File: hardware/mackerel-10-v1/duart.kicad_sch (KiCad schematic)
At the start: 7 parts, among them J10 Conn_01x06, J9 Conn_01x06, U7 XR68C681, X2 3.6864MHz

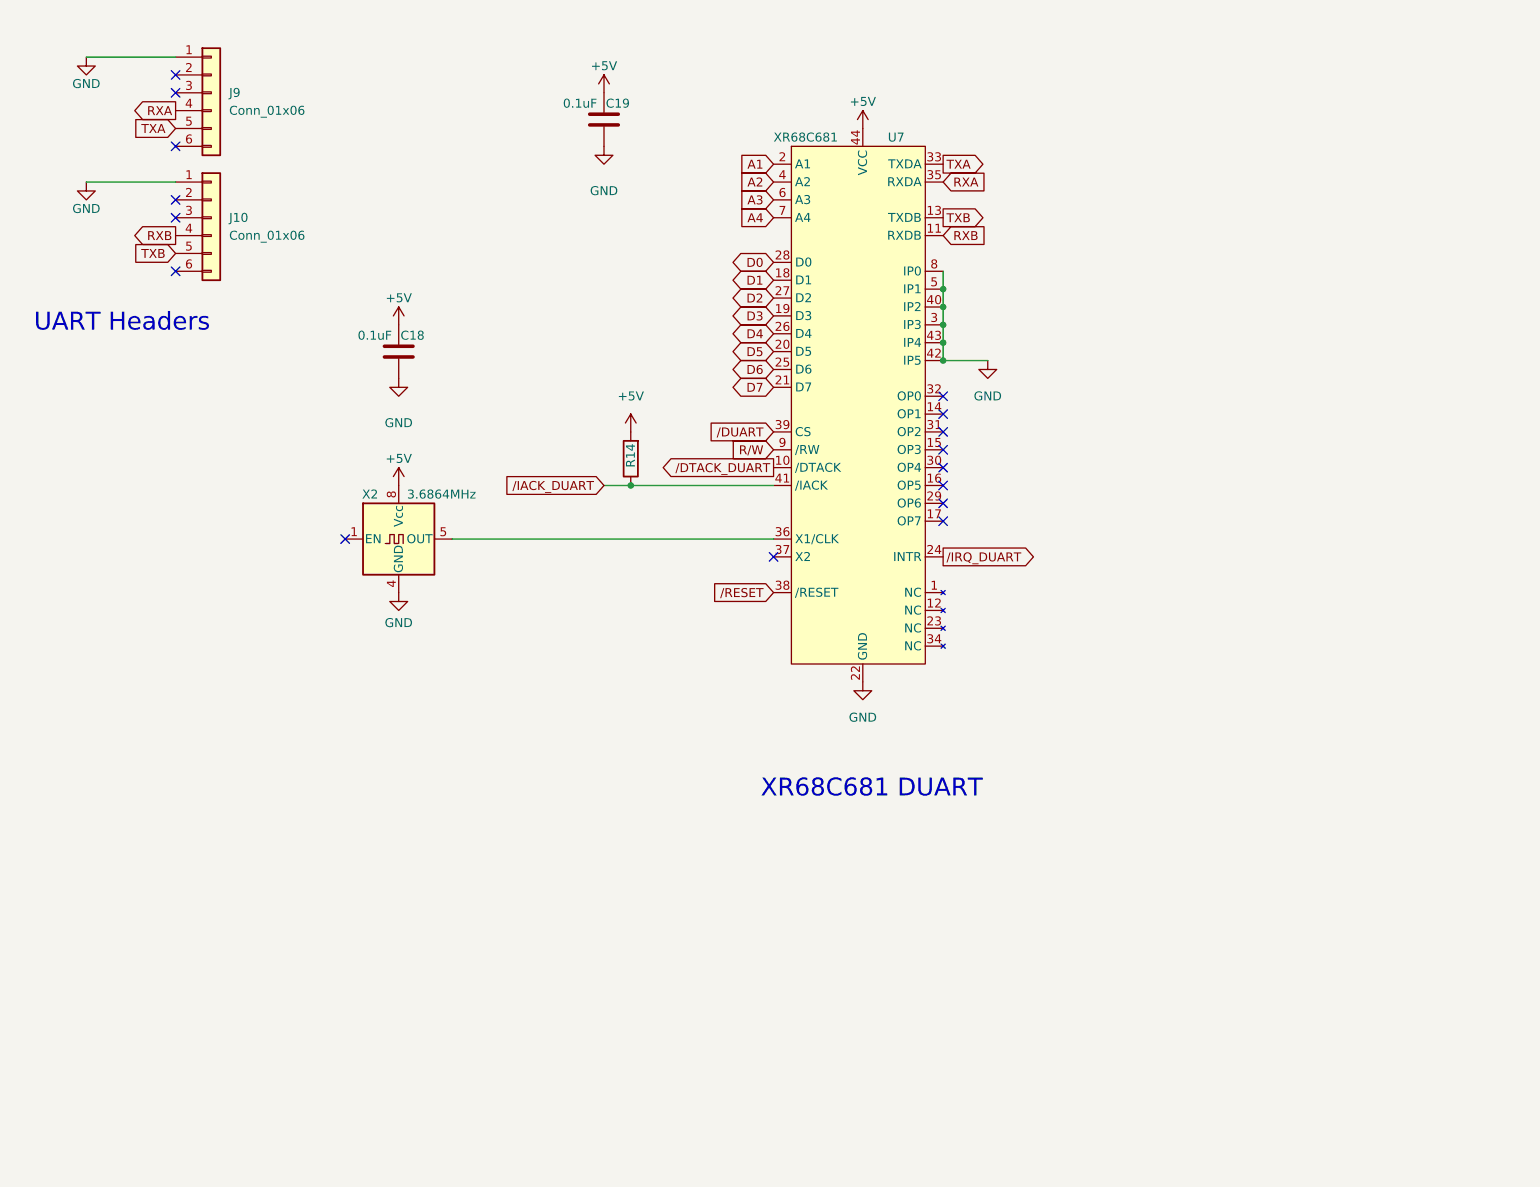
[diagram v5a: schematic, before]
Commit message: Mackerel-10 proto board ready for manufacturing
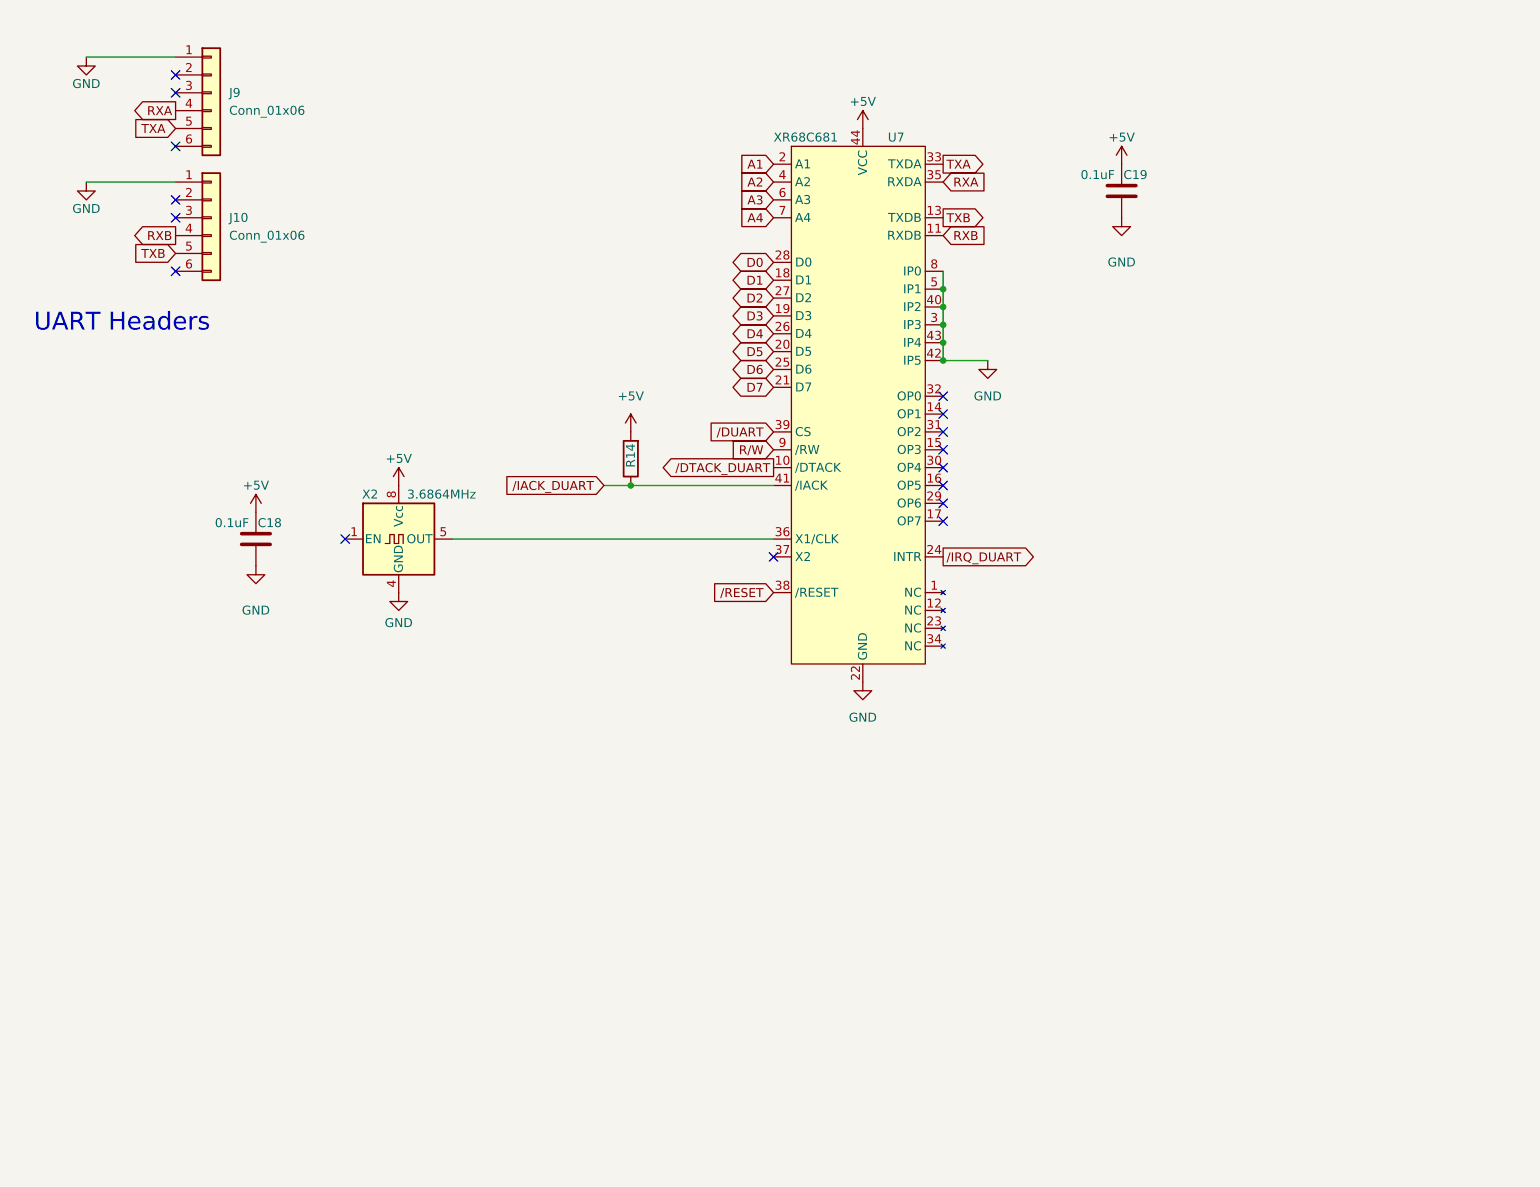
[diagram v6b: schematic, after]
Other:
- note removed: "XR68C681 DUART"
- moved on the sheet: C18, C19
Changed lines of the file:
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@@
-		)
-	)
-	(text "XR68C681 DUART"
-		(exclude_from_sim no)
-		(at 156.21 137.16 0)
-		(effects
-			(font
-				(size 2.54 2.54)
-			)
 		)
 	)
@@
 	(symbol
 		(lib_id "Device:C")
-		(at 88.9 74.93 0)
+		(at 68.58 101.6 0)
 		(unit 1)
 		(exclude_from_sim no)
@@
 		(dnp no)
 		(property "Reference" "C18"
-			(at 89.154 72.644 0)
+			(at 68.834 99.314 0)
 			(effects
 				(font
@@
 		)
 		(property "Value" "0.1uF"
-			(at 83.058 72.644 0)
+			(at 62.738 99.314 0)
 			(effects
 				(font
@@
 		)
 		(property "Footprint" "Capacitor_THT:C_Disc_D4.7mm_W2.5mm_P5.00mm"
-			(at 89.8652 78.74 0)
+			(at 69.5452 105.41 0)
 			(effects
 				(font
@@
 		)
 		(property "Datasheet" "~"
-			(at 88.9 74.93 0)
+			(at 68.58 101.6 0)
 			(effects
 				(font
@@
 		)
 		(property "Description" "Unpolarized capacitor"
-			(at 88.9 74.93 0)
+			(at 68.58 101.6 0)
 			(effects
 				(font
@@
 	(symbol
 		(lib_id "power:+5V")
-		(at 88.9 71.12 0)
+		(at 68.58 97.79 0)
 		(unit 1)
 		(exclude_from_sim no)
@@
 		(fields_autoplaced yes)
 		(property "Reference" "#PWR046"
-			(at 88.9 74.93 0)
+			(at 68.58 101.6 0)
 			(effects
 				(font
@@
 		)
 		(property "Value" "+5V"
-			(at 88.9 67.31 0)
+			(at 68.58 93.98 0)
 			(effects
 				(font
@@
 		)
 		(property "Footprint" ""
-			(at 88.9 71.12 0)
+			(at 68.58 97.79 0)
 			(effects
 				(font
@@
 		)
 		(property "Datasheet" ""
-			(at 88.9 71.12 0)
+			(at 68.58 97.79 0)
 			(effects
 				(font
@@
 		)
 		(property "Description" "Power symbol creates a global label with name \"+5V\""
-			(at 88.9 71.12 0)
+			(at 68.58 97.79 0)
 			(effects
 				(font
@@
 	(symbol
 		(lib_id "power:GND")
-		(at 118.11 45.72 0)
+		(at 191.77 55.88 0)
 		(unit 1)
 		(exclude_from_sim no)
@@
 		(fields_autoplaced yes)
 		(property "Reference" "#PWR068"
-			(at 118.11 52.07 0)
+			(at 191.77 62.23 0)
 			(effects
 				(font
@@
 		)
 		(property "Value" "GND"
-			(at 118.11 52.07 0)
+			(at 191.77 62.23 0)
 			(effects
 				(font
@@
 		)
 		(property "Footprint" ""
-			(at 118.11 45.72 0)
+			(at 191.77 55.88 0)
 			(effects
 				(font
@@
 		)
 		(property "Datasheet" ""
-			(at 118.11 45.72 0)
+			(at 191.77 55.88 0)
 			(effects
 				(font
@@
 		)
 		(property "Description" "Power symbol creates a global label with name \"GND\" , ground"
-			(at 118.11 45.72 0)
+			(at 191.77 55.88 0)
 			(effects
 				(font
@@
 	(symbol
 		(lib_id "power:GND")
-		(at 88.9 78.74 0)
+		(at 68.58 105.41 0)
 		(unit 1)
 		(exclude_from_sim no)
@@
 		(fields_autoplaced yes)
 		(property "Reference" "#PWR047"
-			(at 88.9 85.09 0)
+			(at 68.58 111.76 0)
 			(effects
 				(font
@@
 		)
 		(property "Value" "GND"
-			(at 88.9 85.09 0)
+			(at 68.58 111.76 0)
 			(effects
 				(font
@@
 		)
 		(property "Footprint" ""
-			(at 88.9 78.74 0)
+			(at 68.58 105.41 0)
 			(effects
 				(font
@@
 		)
 		(property "Datasheet" ""
-			(at 88.9 78.74 0)
+			(at 68.58 105.41 0)
 			(effects
 				(font
@@
 		)
 		(property "Description" "Power symbol creates a global label with name \"GND\" , ground"
-			(at 88.9 78.74 0)
+			(at 68.58 105.41 0)
 			(effects
 				(font
@@
 	(symbol
 		(lib_id "Device:C")
-		(at 118.11 41.91 0)
+		(at 191.77 52.07 0)
 		(unit 1)
 		(exclude_from_sim no)
@@
 		(dnp no)
 		(property "Reference" "C19"
-			(at 118.364 39.624 0)
+			(at 192.024 49.784 0)
 			(effects
 				(font
@@
 		)
 		(property "Value" "0.1uF"
-			(at 112.268 39.624 0)
+			(at 185.928 49.784 0)
 			(effects
 				(font
@@
 		)
 		(property "Footprint" "Capacitor_THT:C_Disc_D4.7mm_W2.5mm_P5.00mm"
-			(at 119.0752 45.72 0)
+			(at 192.7352 55.88 0)
 			(effects
 				(font
@@
 		)
 		(property "Datasheet" "~"
-			(at 118.11 41.91 0)
+			(at 191.77 52.07 0)
 			(effects
 				(font
@@
 		)
 		(property "Description" "Unpolarized capacitor"
-			(at 118.11 41.91 0)
+			(at 191.77 52.07 0)
 			(effects
 				(font
@@
 	(symbol
 		(lib_id "power:+5V")
-		(at 118.11 38.1 0)
+		(at 191.77 48.26 0)
 		(unit 1)
 		(exclude_from_sim no)
@@
 		(fields_autoplaced yes)
 		(property "Reference" "#PWR067"
-			(at 118.11 41.91 0)
+			(at 191.77 52.07 0)
 			(effects
 				(font
@@
 		)
 		(property "Value" "+5V"
-			(at 118.11 34.29 0)
+			(at 191.77 44.45 0)
 			(effects
 				(font
@@
 		)
 		(property "Footprint" ""
-			(at 118.11 38.1 0)
+			(at 191.77 48.26 0)
 			(effects
 				(font
@@
 		)
 		(property "Datasheet" ""
-			(at 118.11 38.1 0)
+			(at 191.77 48.26 0)
 			(effects
 				(font
@@
 		)
 		(property "Description" "Power symbol creates a global label with name \"+5V\""
-			(at 118.11 38.1 0)
-			(effects
-				(font
+			(at 191.77 48.26 0)
+			(effects
+				(font
